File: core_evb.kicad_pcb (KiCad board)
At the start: 4 copper layers, 140 x 90 mm, 190 parts, among them J1 DIMM204, J10 S_1P1T, J11 RJ45-HR911130C, J12 PJ-327F, J13 CON_1X40, J14 CON-1X2, J2 DC_SOCKET, J3 MICRO-SD-TF01, J4 CON-16X2, J5 CON_2X20, J6 USB_B_F_X2, J7 USB_B_F_X2, J8 S_1P1T, J9 S_1P1T, Q1 2N7002, Q2 2N7002, Q3 SI2302, Q4 SI2301, Q5 SI2302, Q6 SI2301, U1 MP2307, U10 HLF-W2, U2 LM1117, U3 HDMI, U4 GL850G, U5 HS0038B, U6 HLT1160, U7 APX809, U8 RTL8211E, U9 SGM358, X1 12MHz, X2 25MHz

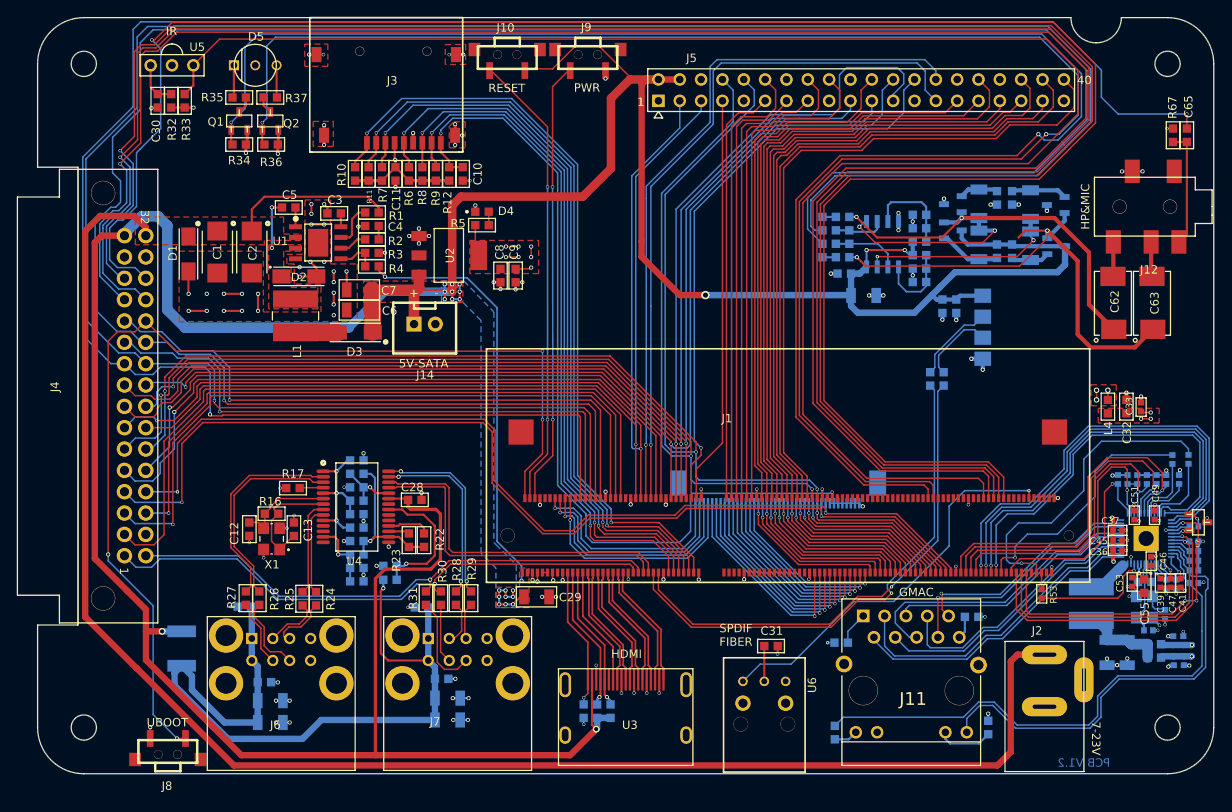
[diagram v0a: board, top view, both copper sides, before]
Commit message: 1.4
Fix some issues
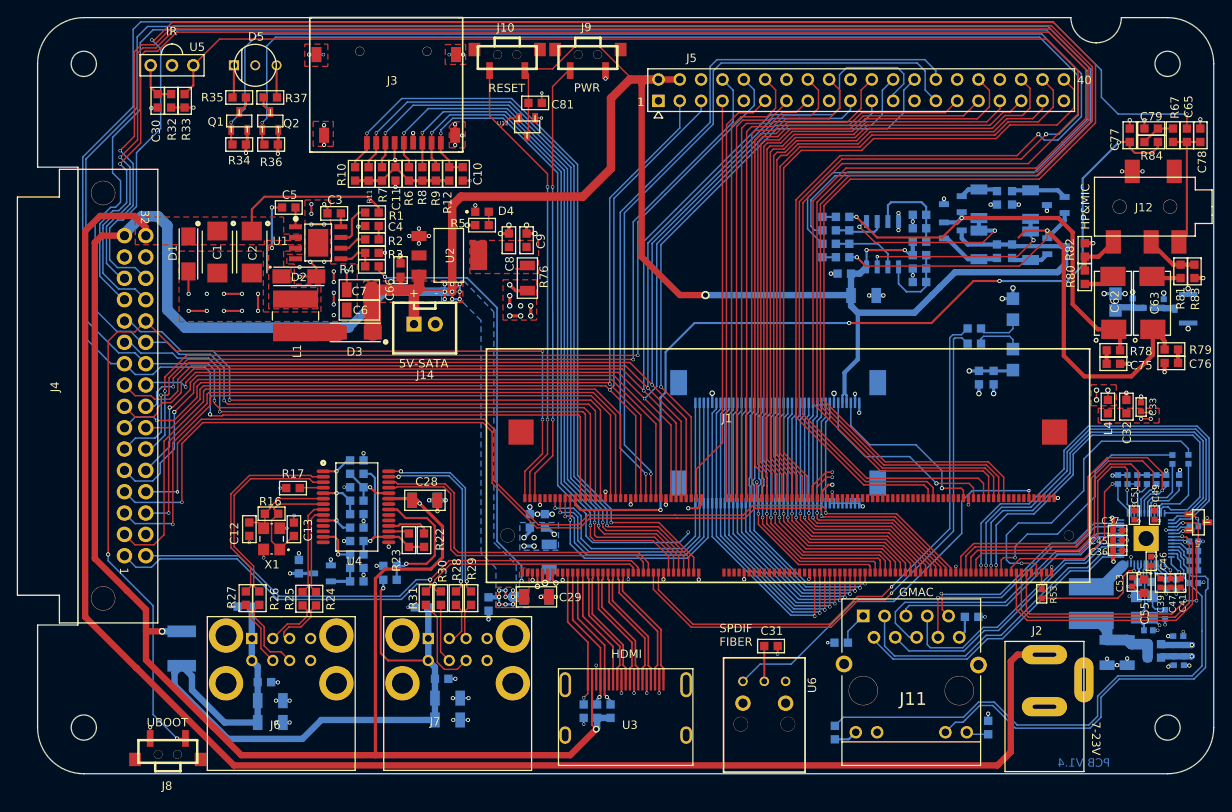
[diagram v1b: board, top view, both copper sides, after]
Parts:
- added C66: 10uF/0603, STD0603, F.Cu at (143.2, 140.1)
- added C68: NC/0402, STD0402, B.Cu at (230.3, 143.9)
- added C69: NC/0402, STD0402, B.Cu at (234.1, 144.1)
- added C70: 22uF/1206, STD1206, B.Cu at (159.4, 178.9)
- added C71: 100nF/0603, STD0603, B.Cu at (153.7, 179.8)
- added C72: 10uF/0603, STD0603, B.Cu at (158.6, 169.9)
- added C73: 10uF/0603, STD0603, B.Cu at (160.4, 169.9)
- added C74: 100nF/0603, STD0603, B.Cu at (131.1, 175.3)
- added C75: 100nF/0603, STD0603, F.Cu at (228.1, 151.2)
- added C76: 100nF/0603, STD0603, F.Cu at (234.9, 151.1)
- added C77: 10uF/0603, STD0603, F.Cu at (230.0, 124.0)
- added C78: NC/10pF/0603, STD0603, F.Cu at (238.4, 124.0)
- added C79: 10uF/0603, STD0603, F.Cu at (232.6, 123.2)
- added C80: 22uF/1206, STD1206, B.Cu at (146.1, 167.4)
- added C81: 100nF/0603, STD0603, F.Cu at (159.2, 120.2)
- added J15: IPX, ipx, B.Cu at (236.9, 144.7)
- added J16: CON_1X40, fpc40_0_5mm_up, B.Cu at (197.8, 155.8)
- added R75: 0R/1206, STD1206, B.Cu at (160.9, 174.2)
- added R76: NC/0R/1206, STD1206, F.Cu at (158.3, 141.0)
- added R77: 0R/0402, STD0402, B.Cu at (232.2, 144.6)
- added R78: 22R/0603, STD0603, F.Cu at (228.1, 149.6)
- added R79: 22R/0603, STD0603, F.Cu at (234.9, 149.5)
- added R80: 0R/0603, STD0603, F.Cu at (224.7, 140.9)
- added R81: 0R/0603, STD0603, F.Cu at (236.1, 140.2)
- added R82: 10KR/0603, STD0603, F.Cu at (224.7, 137.7)
- added R83: 10KR/0603, STD0603, F.Cu at (237.7, 140.2)
- added R84: 100R/0603, STD0603, F.Cu at (232.6, 124.8)
- added U11: APX809, sot_23, B.Cu at (133.8, 176.2)
- added U12: APX810, sot_23, F.Cu at (158.3, 123.0)
- C25: value 100nF/0603 -> 1uF/0603
- C28: value 100nF/0603 -> 22uF/1206; footprint STD0603 -> STD1206
- C65: value 10uF/0603 -> 1uF/0603
- C8: value 1uF/0603 -> 10uF/0603
- R21: value 10KR/0603 -> NC/10KR/0603
- R67: value 10KR/0603 -> 2KR/0603
- U10: value HLF-W2 -> HLF-W12; footprint HLF-W2 -> HLF-W12
- moved G*** 10.9 mm to (160.7, 132.8)
- moved G*** 10.5 mm to (164.8, 145.1)
- moved G*** 10.5 mm to (178.6, 132.2)
- moved C61 9.59 mm to (213.8, 152.8)
- moved C64 9.55 mm to (212.1, 152.8)
- moved R74 7.02 mm to (211.5, 147.0), turned to 180 degrees
- moved R73 6.72 mm to (211.5, 148.8), turned to 180 degrees
- moved U10 4.47 mm to (216.1, 140.4)
- moved C9 4.40 mm to (158.2, 136.5), turned to 90 degrees
- moved C8 4.32 mm to (156.1, 136.5), turned to 90 degrees
- moved C28 1.20 mm to (146.1, 167.4)
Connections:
- net /core/3V3 renamed N-00000129
- C61 pad 1: 5V -> 3V3
- C62 pad 2: /speaker&mic/HPLOUT -> N-00000221
- C63 pad 2: /speaker&mic/HPROUT -> N-00000222
- C64 pad 1: 5V -> 3V3
- C8 pad 1: 3V3 -> N-00000140
- C9 pad 1: 3V3 -> N-00000140
- J1 pad 168: (no net) -> PH27
- J1 pad 172: (no net) -> PB2
- J1 pad 22: (no net) -> VMIC
- J11 pad 13: N-00000193 -> /gmac/LED0
- J11 pad 14: /gmac/LED0 -> N-00000213
- R56 pad 1: N-00000193 -> N-00000213
- R67 pad 1: 3V3 -> N-00000226
- U10 pad 1: 5V -> 3V3
- U2 pad 4: 3V3 -> N-00000140
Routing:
- net VMIC: track 0.00 -> 107.1 mm, vias 0 -> 4
- net GND: track 177.6 -> 215.7 mm, vias 152 -> 180
- net PB2: track 0.00 -> 23.4 mm, vias 0 -> 1
- net PH27: track 0.00 -> 21.5 mm, vias 0 -> 1
- net 5V: track 495.8 -> 515.4 mm, vias 25 -> 26
- net LCD0_D11: track 18.7 -> 31.0 mm
- net LCD0_D10: track 20.4 -> 32.7 mm
- net LCD0_D12: track 19.0 -> 31.3 mm
- net LCD0_D13: track 19.2 -> 31.5 mm
- net LCD0_D9: track 21.0 -> 33.3 mm
- net LCD0_D4: track 23.5 -> 35.6 mm
- net LCD0_D7: track 22.0 -> 34.2 mm
- net LCD0_D5: track 23.0 -> 35.1 mm
- net LCD0_D21: track 19.4 -> 31.6 mm
- net LCD0_D20: track 19.4 -> 31.6 mm
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- added copper zone on B.Cu, net 3V3
- added copper zone on F.Cu, net N-00000140
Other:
- board text added: "PCB V1.4"
- board text removed: "PCB V1.2"
